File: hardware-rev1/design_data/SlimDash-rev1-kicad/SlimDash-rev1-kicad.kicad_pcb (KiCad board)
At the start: 2 copper layers, 157.1 x 131.5 mm, 140 parts, among them J1 AudioJack4, J2 AudioJack4, U1 TLV73333PDBV, U2 RP2040, U3 W25Q128JVS, Y1 Crystal_GND24

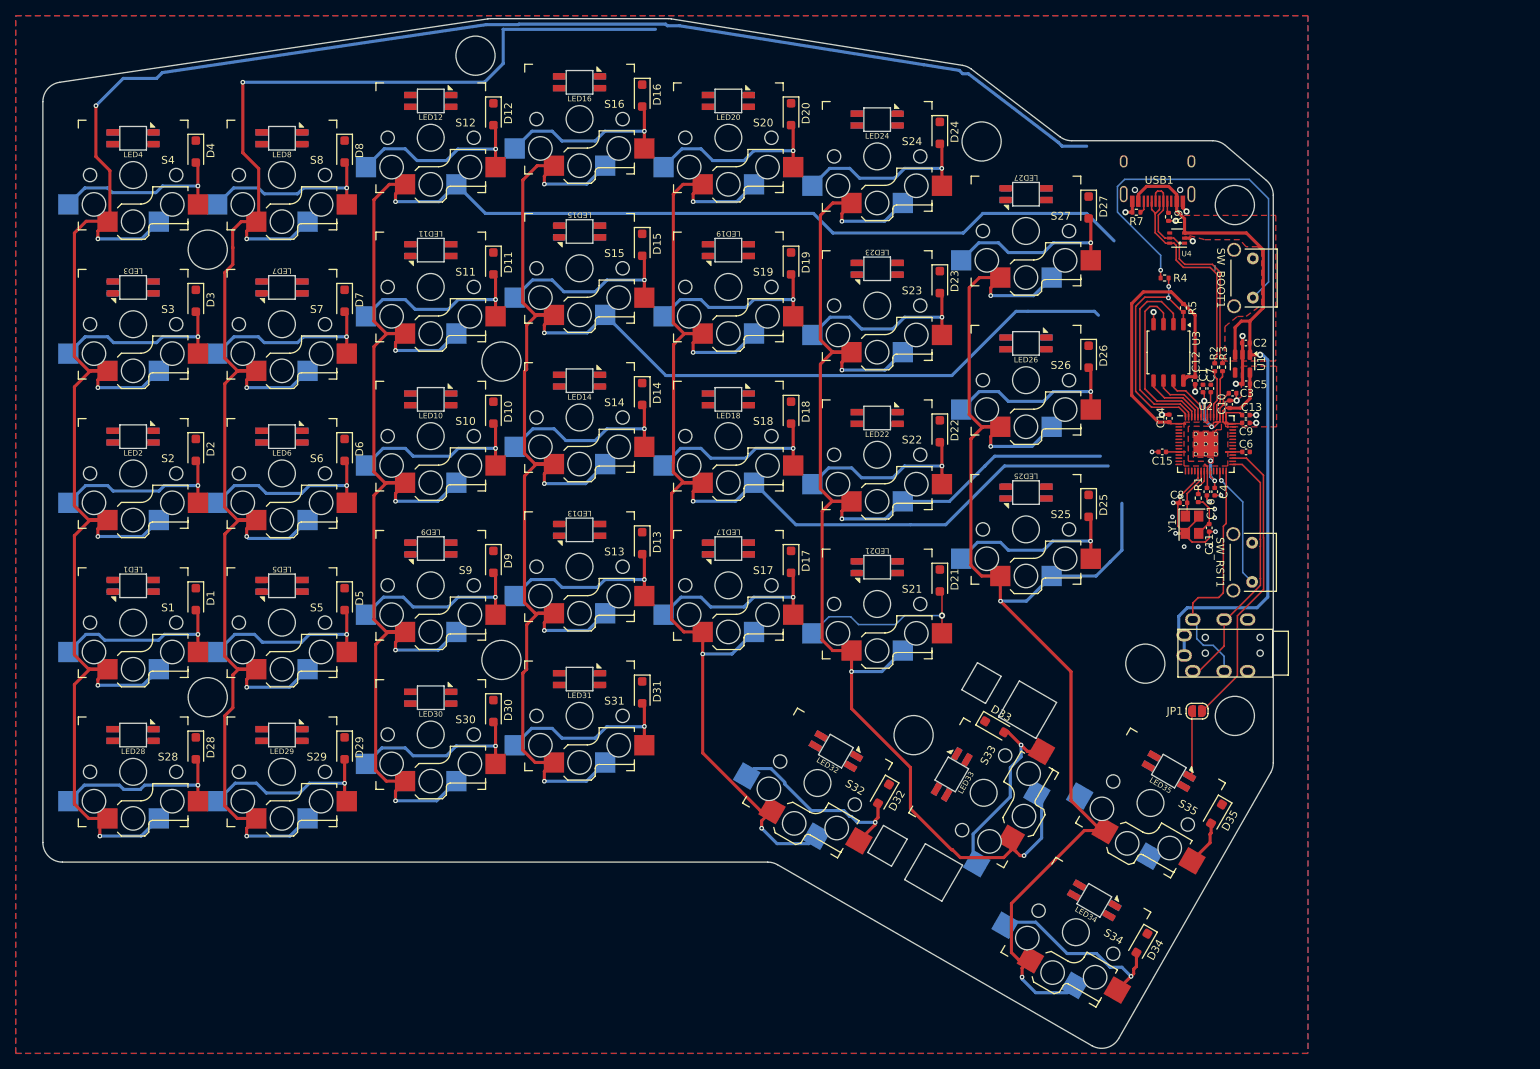
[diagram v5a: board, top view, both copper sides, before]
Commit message: more routing and fixing footprints
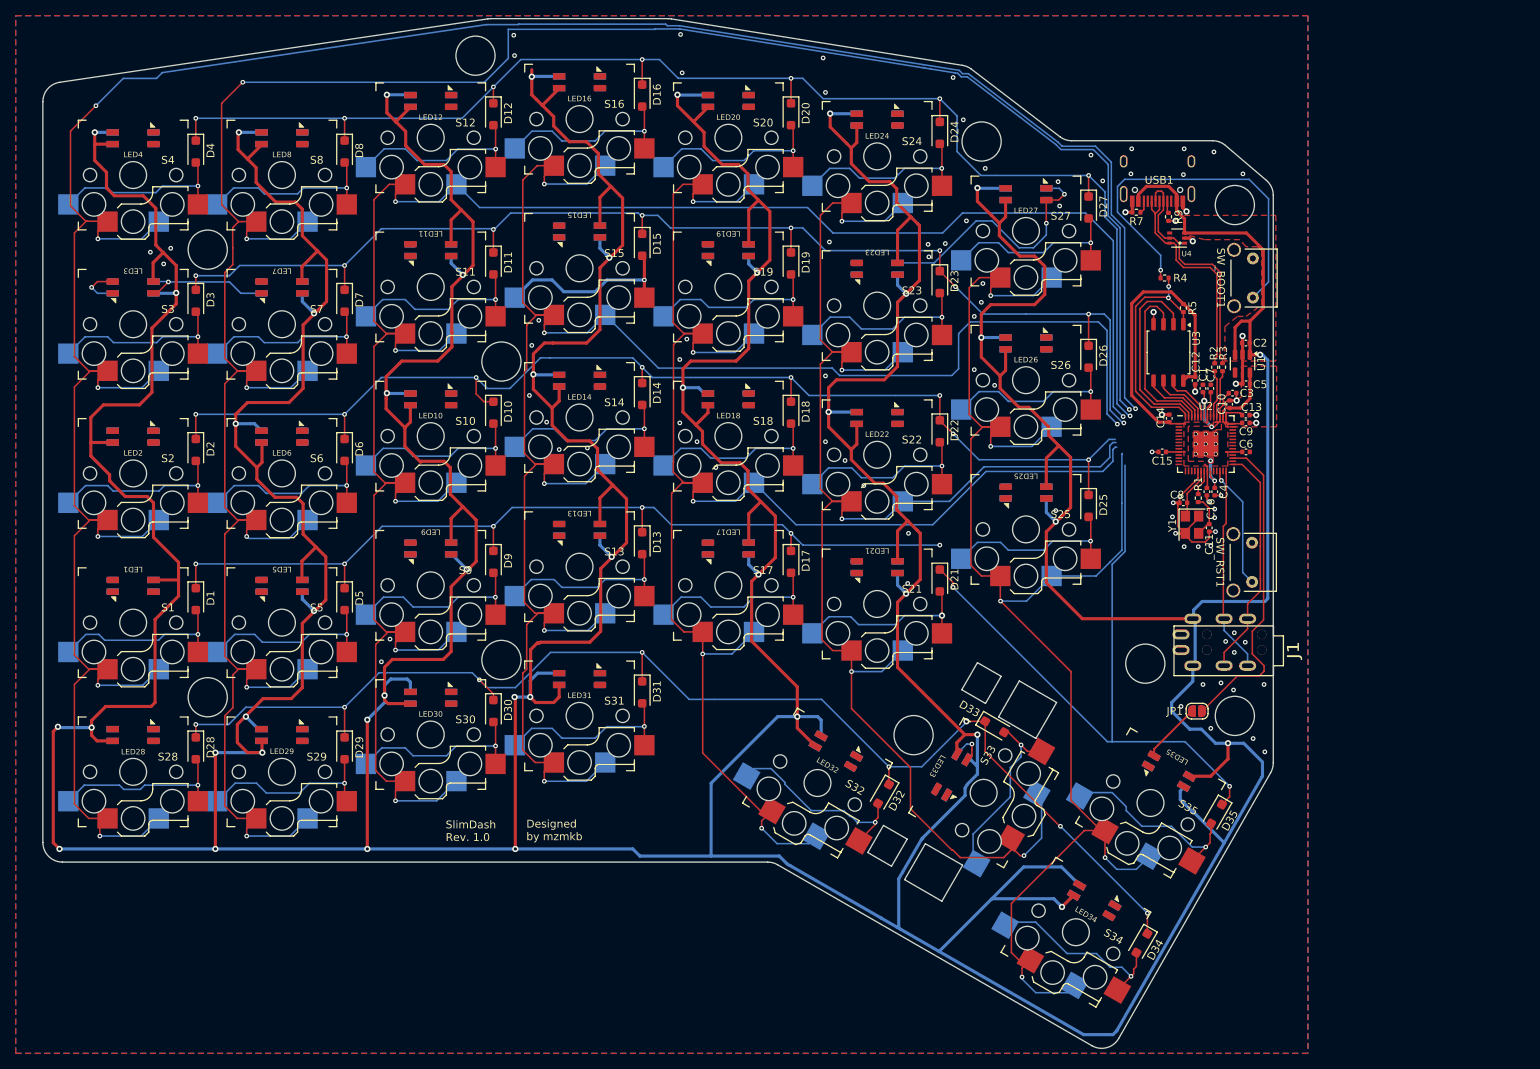
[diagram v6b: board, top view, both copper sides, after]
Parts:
- J1, J2: footprint Keebio-Parts:TRRS-PJ-320A -> mzm_misc:TRRS_jack
- moved J2 2.40 mm to (195.6, 99.5)
- moved J1 1.60 mm to (195.6, 105.5)
- turned LED27 to 0 degrees
- turned LED33 to -120 degrees
- turned LED35 to 150 degrees
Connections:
- LED1 pad 1: Net-(LED1-DOUT) -> +5V
- LED1 pad 2: GND -> Net-(LED1-DOUT)
- LED1 pad 3: Net-(LED1-DIN) -> GND
- LED1 pad 4: +5V -> Net-(LED1-DIN)
- LED10 pad 1: Net-(LED10-DOUT) -> +5V
- LED10 pad 2: GND -> Net-(LED10-DOUT)
- LED10 pad 3: Net-(LED10-DIN) -> GND
- LED10 pad 4: +5V -> Net-(LED10-DIN)
- LED11 pad 1: Net-(LED11-DOUT) -> +5V
- LED11 pad 2: GND -> Net-(LED11-DOUT)
- LED11 pad 3: Net-(LED11-DIN) -> GND
- LED11 pad 4: +5V -> Net-(LED11-DIN)
- LED12 pad 1: Net-(LED12-DOUT) -> +5V
- LED12 pad 2: GND -> Net-(LED12-DOUT)
- LED12 pad 3: Net-(LED12-DIN) -> GND
- LED12 pad 4: +5V -> Net-(LED12-DIN)
- LED13 pad 1: Net-(LED13-DOUT) -> +5V
- LED13 pad 2: GND -> Net-(LED13-DOUT)
- LED13 pad 3: Net-(LED13-DIN) -> GND
- LED13 pad 4: +5V -> Net-(LED13-DIN)
- LED14 pad 1: Net-(LED10-DIN) -> +5V
- LED14 pad 2: GND -> Net-(LED10-DIN)
- LED14 pad 3: Net-(LED14-DIN) -> GND
- LED14 pad 4: +5V -> Net-(LED14-DIN)
- LED15 pad 1: Net-(LED15-DOUT) -> +5V
- LED15 pad 2: GND -> Net-(LED15-DOUT)
- LED15 pad 3: Net-(LED11-DOUT) -> GND
- LED15 pad 4: +5V -> Net-(LED11-DOUT)
- LED16 pad 1: Net-(LED12-DIN) -> +5V
- LED16 pad 2: GND -> Net-(LED12-DIN)
- LED16 pad 3: Net-(LED16-DIN) -> GND
- LED16 pad 4: +5V -> Net-(LED16-DIN)
- LED17 pad 1: Net-(LED17-DOUT) -> +5V
- LED17 pad 2: GND -> Net-(LED17-DOUT)
- LED17 pad 3: Net-(LED13-DOUT) -> GND
- LED17 pad 4: +5V -> Net-(LED13-DOUT)
- LED18 pad 1: Net-(LED14-DIN) -> +5V
- LED18 pad 2: GND -> Net-(LED14-DIN)
- LED18 pad 3: Net-(LED18-DIN) -> GND
- LED18 pad 4: +5V -> Net-(LED18-DIN)
- LED19 pad 1: Net-(LED19-DOUT) -> +5V
- LED19 pad 2: GND -> Net-(LED19-DOUT)
- LED19 pad 3: Net-(LED15-DOUT) -> GND
- LED19 pad 4: +5V -> Net-(LED15-DOUT)
- LED2 pad 1: Net-(LED2-DOUT) -> +5V
- LED2 pad 2: GND -> Net-(LED2-DOUT)
- LED2 pad 3: Net-(LED2-DIN) -> GND
- LED2 pad 4: +5V -> Net-(LED2-DIN)
- LED20 pad 1: Net-(LED16-DIN) -> +5V
- LED20 pad 2: GND -> Net-(LED16-DIN)
- LED20 pad 3: Net-(LED20-DIN) -> GND
- LED20 pad 4: +5V -> Net-(LED20-DIN)
- LED21 pad 1: Net-(LED21-DOUT) -> +5V
- LED21 pad 2: GND -> Net-(LED21-DOUT)
- LED21 pad 3: Net-(LED17-DOUT) -> GND
- LED21 pad 4: +5V -> Net-(LED17-DOUT)
- LED22 pad 1: Net-(LED18-DIN) -> +5V
- LED22 pad 2: GND -> Net-(LED18-DIN)
- LED22 pad 3: Net-(LED22-DIN) -> GND
- LED22 pad 4: +5V -> Net-(LED22-DIN)
- LED23 pad 1: Net-(LED23-DOUT) -> +5V
- LED23 pad 2: GND -> Net-(LED23-DOUT)
- LED23 pad 3: Net-(LED19-DOUT) -> GND
- LED23 pad 4: +5V -> Net-(LED19-DOUT)
- LED24 pad 1: Net-(LED20-DIN) -> +5V
- LED24 pad 2: GND -> Net-(LED20-DIN)
- LED24 pad 3: Net-(LED24-DIN) -> GND
- LED24 pad 4: +5V -> Net-(LED24-DIN)
- LED25 pad 1: Net-(LED25-DOUT) -> +5V
- LED25 pad 2: GND -> Net-(LED25-DOUT)
- LED25 pad 3: Net-(LED21-DOUT) -> GND
- LED25 pad 4: +5V -> Net-(LED21-DOUT)
- LED26 pad 1: Net-(LED22-DIN) -> +5V
- LED26 pad 2: GND -> Net-(LED22-DIN)
- LED26 pad 3: Net-(LED25-DOUT) -> GND
- LED26 pad 4: +5V -> Net-(LED25-DOUT)
- LED27 pad 1: Net-(LED24-DIN) -> +5V
- LED27 pad 2: GND -> Net-(LED24-DIN)
- LED27 pad 3: Net-(LED23-DOUT) -> GND
- LED27 pad 4: +5V -> Net-(LED23-DOUT)
- LED28 pad 1: Net-(LED1-DIN) -> +5V
- LED28 pad 2: GND -> Net-(LED1-DIN)
- LED28 pad 3: Net-(LED28-DIN) -> GND
- LED28 pad 4: +5V -> Net-(LED28-DIN)
- LED29 pad 1: Net-(LED28-DIN) -> +5V
- LED29 pad 2: GND -> Net-(LED28-DIN)
- LED29 pad 3: Net-(LED29-DIN) -> GND
- LED29 pad 4: +5V -> Net-(LED29-DIN)
- LED3 pad 1: Net-(LED3-DOUT) -> +5V
- LED3 pad 2: GND -> Net-(LED3-DOUT)
- LED3 pad 3: Net-(LED2-DOUT) -> GND
- LED3 pad 4: +5V -> Net-(LED2-DOUT)
- LED30 pad 1: Net-(LED29-DIN) -> +5V
- LED30 pad 2: GND -> Net-(LED29-DIN)
- LED30 pad 3: Net-(LED30-DIN) -> GND
- LED30 pad 4: +5V -> Net-(LED30-DIN)
- LED31 pad 1: Net-(LED30-DIN) -> +5V
- LED31 pad 2: GND -> Net-(LED30-DIN)
- LED31 pad 3: Net-(LED31-DIN) -> GND
- LED31 pad 4: +5V -> Net-(LED31-DIN)
- LED32 pad 1: Net-(LED31-DIN) -> +5V
- LED32 pad 2: GND -> Net-(LED31-DIN)
- LED32 pad 3: Net-(LED32-DIN) -> GND
- LED32 pad 4: +5V -> Net-(LED32-DIN)
- LED33 pad 1: Net-(LED32-DIN) -> +5V
- LED33 pad 2: GND -> Net-(LED32-DIN)
- LED33 pad 3: Net-(LED33-DIN) -> GND
- LED33 pad 4: +5V -> Net-(LED33-DIN)
- LED34 pad 1: Net-(LED33-DIN) -> +5V
- LED34 pad 2: GND -> Net-(LED33-DIN)
- LED34 pad 3: Net-(LED34-DIN) -> GND
- LED34 pad 4: +5V -> Net-(LED34-DIN)
- LED35 pad 1: Net-(LED34-DIN) -> +5V
- LED35 pad 2: GND -> Net-(LED34-DIN)
- LED35 pad 3: Net-(JP1-B) -> GND
- LED35 pad 4: +5V -> Net-(JP1-B)
- LED4 pad 1: unconnected-(LED4-DOUT-Pad1)_1 -> +5V
- LED4 pad 2: GND -> unconnected-(LED4-DOUT-Pad2)_1
- LED4 pad 3: Net-(LED4-DIN) -> GND
- LED4 pad 4: +5V -> Net-(LED4-DIN)
- LED5 pad 1: Net-(LED5-DOUT) -> +5V
- LED5 pad 2: GND -> Net-(LED5-DOUT)
- LED5 pad 3: Net-(LED1-DOUT) -> GND
- LED5 pad 4: +5V -> Net-(LED1-DOUT)
- LED6 pad 1: Net-(LED2-DIN) -> +5V
- LED6 pad 2: GND -> Net-(LED2-DIN)
- LED6 pad 3: Net-(LED10-DOUT) -> GND
- LED6 pad 4: +5V -> Net-(LED10-DOUT)
- LED7 pad 1: Net-(LED11-DIN) -> +5V
- LED7 pad 2: GND -> Net-(LED11-DIN)
- LED7 pad 3: Net-(LED3-DOUT) -> GND
- LED7 pad 4: +5V -> Net-(LED3-DOUT)
- LED8 pad 1: Net-(LED4-DIN) -> +5V
- LED8 pad 2: GND -> Net-(LED4-DIN)
- LED8 pad 3: Net-(LED12-DOUT) -> GND
- LED8 pad 4: +5V -> Net-(LED12-DOUT)
- LED9 pad 1: Net-(LED13-DIN) -> +5V
- LED9 pad 2: GND -> Net-(LED13-DIN)
- LED9 pad 3: Net-(LED5-DOUT) -> GND
- LED9 pad 4: +5V -> Net-(LED5-DOUT)
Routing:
- net +5V: track 93.2 -> 1443.5 mm, vias 1 -> 43
- net ROW3: track 0.32 -> 202.6 mm, vias 0 -> 8
- net ROW0: track 0.00 -> 179.0 mm, vias 0 -> 8
- net ROW4: track 0.00 -> 165.3 mm, vias 0 -> 8
- net ROW1: track 0.00 -> 158.7 mm, vias 0 -> 9
- net ROW2: track 0.00 -> 150.5 mm, vias 0 -> 8
- net COL1: track 235.8 -> 332.1 mm, vias 6 -> 7
- net COL0: track 307.4 -> 346.0 mm, vias 6 -> 7
- net Net-(LED23-DOUT): track 0.00 -> 33.1 mm, vias 0 -> 2
- net COL2: track 246.9 -> 269.8 mm, vias 5 -> 6
- net GND: track 43.3 -> 65.8 mm, vias 25 -> 89
- net Net-(D35-A): track 5.78 -> 25.2 mm, vias 0 -> 1
- net Net-(LED3-DOUT): track 0.00 -> 17.1 mm, vias 0 -> 1
- net COL6: track 171.7 -> 188.5 mm, vias 4 -> 5
- net COL3: track 227.5 -> 243.4 mm, vias 5 -> 6
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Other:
- board text added: "Designed by mzmkb"
- board text added: "SlimDash Rev. 1.0"
